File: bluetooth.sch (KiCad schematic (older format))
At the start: 63 parts, among them P16 CONN_2, P17 CONN_1, P18 CONN_1, P19 CONN_1, P20 CONN_1, P21 CONN_1, P22 CONN_1, P23 CONN_1, P24 CONN_1, P25 CONN_1, P28 CONN_1, P29 CONN_1, P30 CONN_1, P5 CONN_1, P6 CONN_1, Q1 MOSFET_N, Q3 MOSFET_N, Q4 MOS_P, Q5 MOS_P, SW3 DPST, U2 TAR5SB33, U3 HT7750A, U4 LTC4054, U5 RN42

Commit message: Add footprint of PPTC and SOD123
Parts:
- removed D2: MA721, symbol DIODE_SCHOTTKY_SOT23
- D2: renamed from D4; value RB521 -> Schottky
- renumbered D5 to D3, D3 to D4, D6 to D5, D7 to D6, D8 to D7, D9 to D8, R14 to R13, R13 to R14
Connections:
- wire segments 157 -> 153
- no-connect marks 17 -> 16
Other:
- note added: "Alt: NCP1402"
- note removed: "Schottky 30V 1A"
- moved on the sheet: D2
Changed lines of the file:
@@
 Roving Networks RN42
 $Comp
-L LED D3
+L LED D4
 U 1 1 51B43D8A
 P 5000 6400
-F 0 "D3" H 5000 6500 50  0000 C CNN
+F 0 "D4" H 5000 6500 50  0000 C CNN
 F 1 "LED" H 5000 6300 50  0000 C CNN
 F 2 "" H 5000 6400 60  0000 C CNN
@@
 Text Notes 750  4250 0    60   ~ 0
 5V Output
-NoConn ~ 2950 4350
 $Comp
 L CONN_1 P21
@@
 	1    0    0    -1
 $EndComp
-Text Notes 3900 4050 2    60   ~ 0
-Schottky 30V 1A
-$Comp
-L DIODESCH D4
+$Comp
+L DIODESCH D2
 U 1 1 51B973BC
-P 2750 3950
-F 0 "D4" H 2750 4050 40  0000 C CNN
-F 1 "RB521" H 2750 3850 40  0000 C CNN
-F 2 "" H 2750 3950 60  0000 C CNN
-F 3 "" H 2750 3950 60  0000 C CNN
-	1    2750 3950
+P 2750 4450
+F 0 "D2" H 2750 4550 40  0000 C CNN
+F 1 "Schottky" H 2750 4350 40  0000 C CNN
+F 2 "" H 2750 4450 60  0000 C CNN
+F 3 "" H 2750 4450 60  0000 C CNN
+	1    2750 4450
 	-1   0    0    1
 $EndComp
-Text Notes 4000 4200 2    60   ~ 0
-※Select one of two
-$Comp
-L LED D5
+$Comp
+L LED D3
 U 1 1 51B997A0
 P 4700 6400
-F 0 "D5" H 4700 6500 50  0000 C CNN
+F 0 "D3" H 4700 6500 50  0000 C CNN
 F 1 "LED" H 4700 6300 50  0000 C CNN
 F 2 "" H 4700 6400 60  0000 C CNN
@@
 Amp Measure
 $Comp
-L LED D6
+L LED D5
 U 1 1 51BC0B79
 P 9850 3150
-F 0 "D6" H 9850 3250 50  0000 C CNN
+F 0 "D5" H 9850 3250 50  0000 C CNN
 F 1 "LED" H 9850 3050 50  0000 C CNN
 F 2 "" H 9850 3150 60  0000 C CNN
@@
 $EndComp
 $Comp
-L LED D7
+L LED D6
 U 1 1 51BC0DCE
 P 10150 3150
-F 0 "D7" H 10150 3250 50  0000 C CNN
+F 0 "D6" H 10150 3250 50  0000 C CNN
 F 1 "LED" H 10150 3050 50  0000 C CNN
 F 2 "" H 10150 3150 60  0000 C CNN
@@
 $EndComp
 $Comp
-L R R14
+L R R13
 U 1 1 52B7F726
 P 9850 2600
-F 0 "R14" V 9930 2600 50  0000 C CNN
+F 0 "R13" V 9930 2600 50  0000 C CNN
 F 1 "470" V 9850 2600 50  0000 C CNN
 F 2 "" H 9850 2600 60  0000 C CNN
@@
 $EndComp
 $Comp
-L R R13
+L R R14
 U 1 1 52B7F735
 P 10750 2600
-F 0 "R13" V 10830 2600 50  0000 C CNN
+F 0 "R14" V 10830 2600 50  0000 C CNN
 F 1 "470" V 10750 2600 50  0000 C CNN
 F 2 "" H 10750 2600 60  0000 C CNN
@@
 $EndComp
 $Comp
-L LED D8
+L LED D7
 U 1 1 52B7FA89
 P 10750 3150
-F 0 "D8" H 10750 3250 50  0000 C CNN
+F 0 "D7" H 10750 3250 50  0000 C CNN
 F 1 "LED" H 10750 3050 50  0000 C CNN
 F 2 "" H 10750 3150 60  0000 C CNN
@@
 $EndComp
 $Comp
-L LED D9
+L LED D8
 U 1 1 52B7FA8F
 P 11050 3150
-F 0 "D9" H 11050 3250 50  0000 C CNN
+F 0 "D8" H 11050 3250 50  0000 C CNN
 F 1 "LED" H 11050 3050 50  0000 C CNN
 F 2 "" H 11050 3150 60  0000 C CNN
@@
 Text Notes 700  7250 0    60   ~ 0
 USB connected: VUSB\nUSB not connected: LIPO
-$Comp
-L DIODE_SCHOTTKY_SOT23 D2
-U 1 1 51B567E3
-P 2750 4450
-F 0 "D2" H 2750 4550 40  0000 C CNN
-F 1 "MA721" H 2800 4200 40  0000 C CNN
-F 2 "" H 2750 4450 60  0000 C CNN
-F 3 "" H 2750 4450 60  0000 C CNN
-	1    2750 4450
-	-1   0    0    1
-$EndComp
 Text Notes 6050 6400 2    60   ~ 0
 ※Select one of two
@@
 Wire Wire Line
 	3950 6350 4550 6350
-Connection ~ 2350 4450
-Wire Wire Line
-	2350 3950 2350 4450
-Wire Wire Line
-	2550 3950 2350 3950
-Connection ~ 3100 4450
-Wire Wire Line
-	3100 3950 3100 4450
-Wire Wire Line
-	2950 3950 3100 3950
 Wire Wire Line
 	6500 7400 6500 7450
@@
 Text Notes 10000 5400 0    60   ~ 0
 On: Bluetooth mode\nOff: USB mode or BT off
+Text Notes 2400 5250 0    60   ~ 0
+Alt: NCP1402
 $EndSCHEMATC

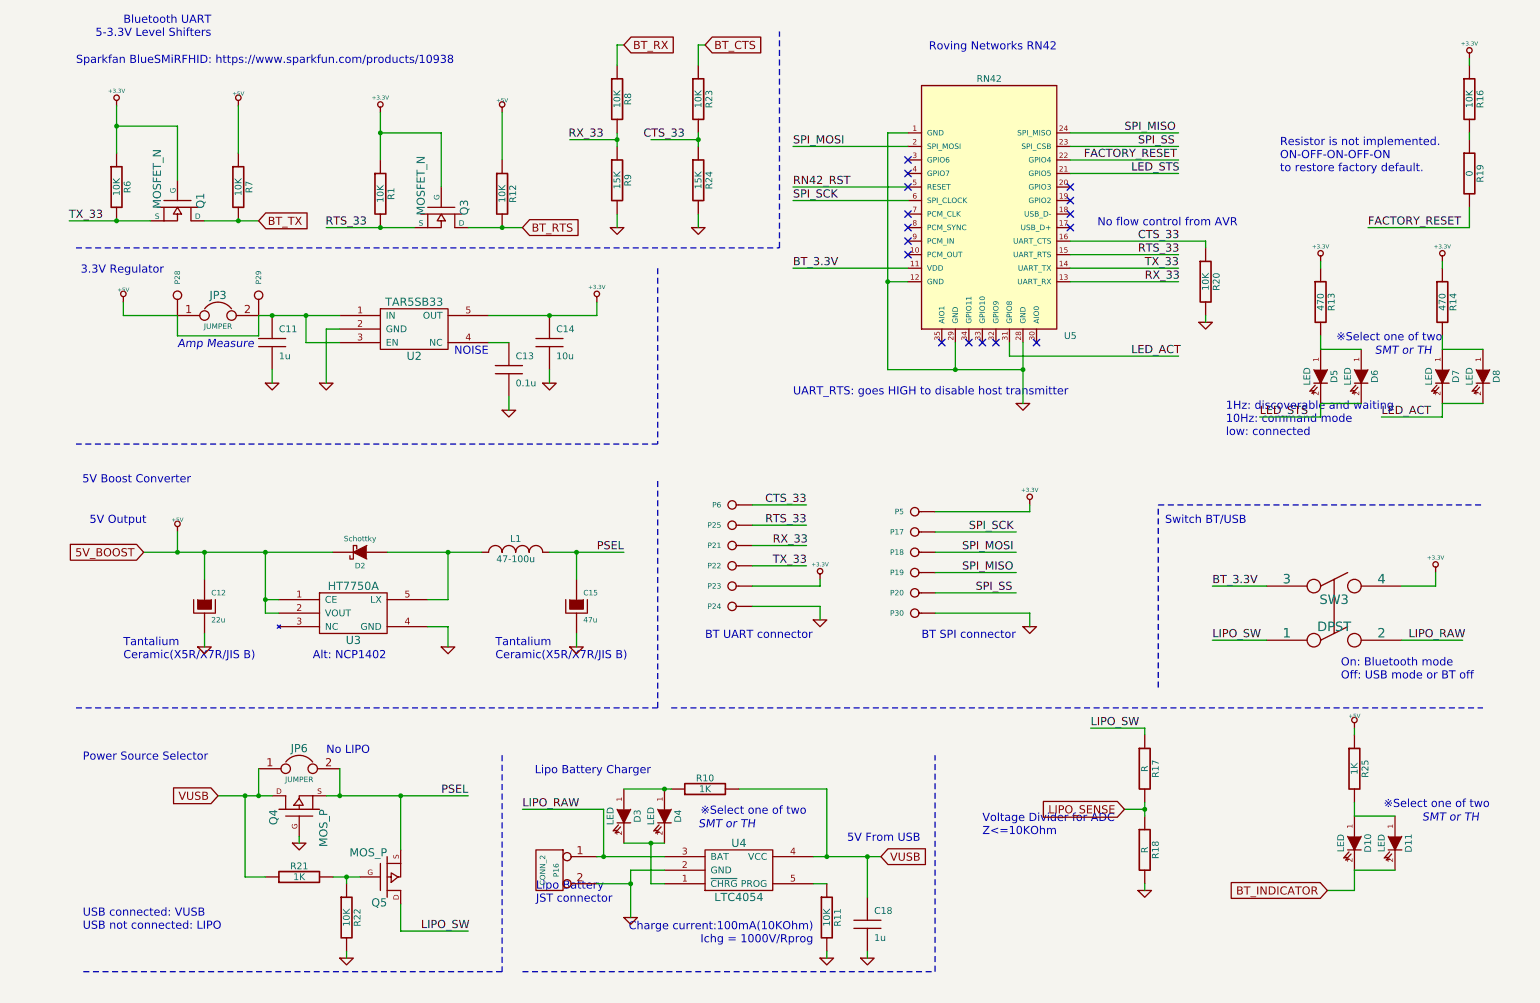
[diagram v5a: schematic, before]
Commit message: Design initial Rev.B PCB
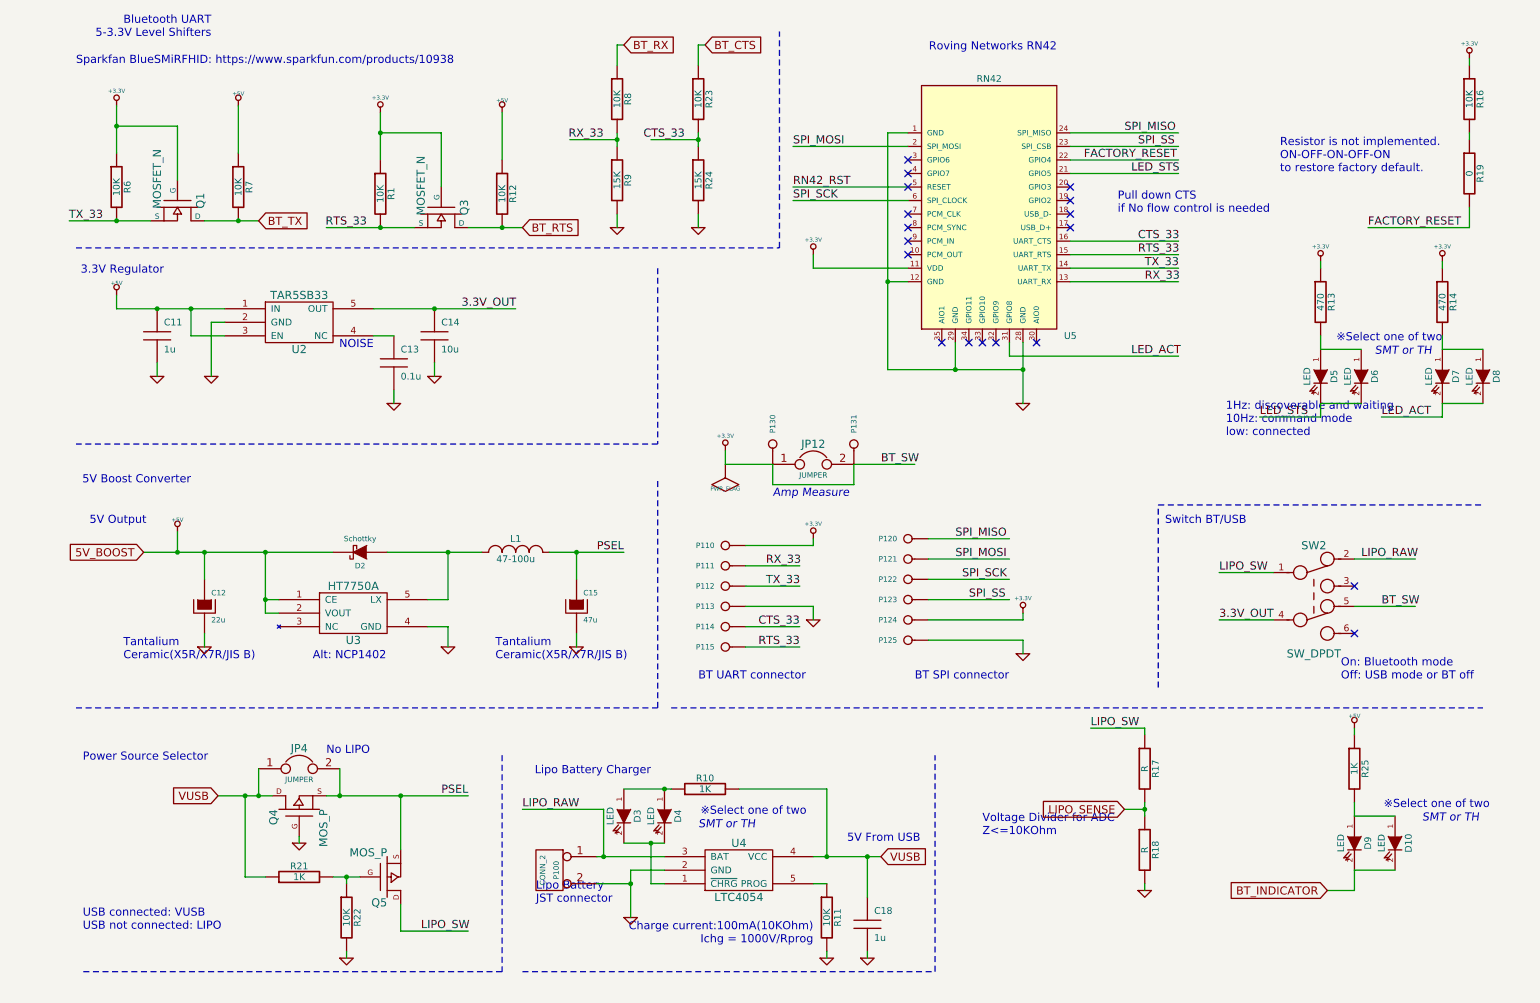
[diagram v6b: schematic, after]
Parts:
- removed R20: 10K, symbol R
- removed SW3: DPST, symbol DPST
- added SW2: SW_DPDT, symbol SW_DPDT
- renumbered D11 to D10, D10 to D9, JP3 to JP12, JP6 to JP4, P16 to P100, P23 to P110, P21 to P111, P22 to P112, P24 to P113, P6 to P114, P25 to P115, P19 to P120, P18 to P121, P17 to P122, P20 to P123, P5 to P124, P30 to P125, P28 to P130, P29 to P131
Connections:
- net labels added: 3.3V_OUT, BT_SW
- net labels removed: BT_3.3V
- wire segments 153 -> 152
- no-connect marks 16 -> 18
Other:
- note added: "Pull down CTS\nif No flow control is needed"
- note removed: "No flow control from AVR"
- note removed: "UART_RTS: goes HIGH to disable host transmitter"
- moved on the sheet: C11, C13, C14, JP12, P110, P111, P112, P113, P114, P115, P120, P121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

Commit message: Fix many fixes of rev.B errata
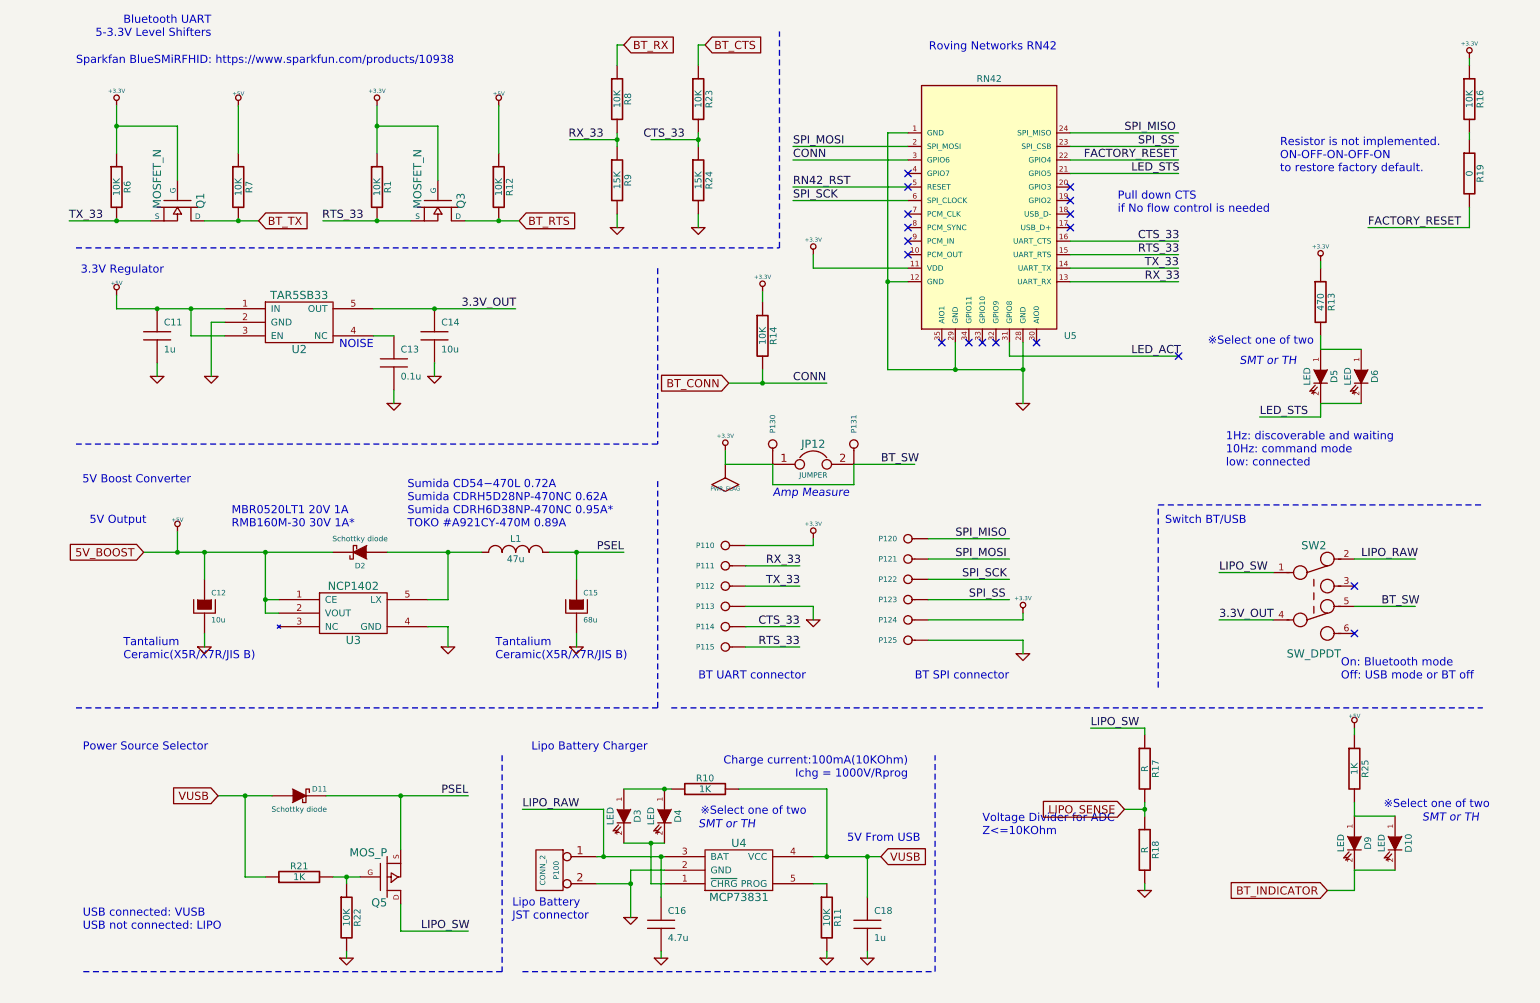
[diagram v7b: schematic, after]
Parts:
- removed D7, D8: LED, symbol LED
- removed JP4: JUMPER, symbol JUMPER
- removed Q4: MOS_P, symbol MOS_P
- added C16: 4.7u, symbol C
- added D11: Schottky diode, symbol DIODESCH
- C12: value 22u -> 10u
- C15: value 47u -> 68u
- D2: value Schottky -> Schottky diode
- L1: value 47-100u -> 47u
- R14: value 470 -> 10K
- U3: value HT7750A -> NCP1402
- U4: value LTC4054 -> MCP73831
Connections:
- net labels added: BT_CONN, CONN
- wire segments 152 -> 149
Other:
- note added: "MBR0520LT1 20V 1A\nRMB160M-30 30V 1A*"
- note added: "Sumida CD54−470L 0.72A\nSumida CDRH5D28NP-470NC 0.62A\nSumida CDRH6D38NP-470NC 0.95A*\nTOKO #A921CY-470M 0.89A"
- note removed: "Alt: NCP1402"
- note removed: "No LIPO"
- moved on the sheet: Q3, R1, R12

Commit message: Change for rev.C
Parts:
- removed D6: LED, symbol LED
- removed P120, P121, P122, P123, P124, P125: CONN_1, symbol CONN_1
- added R20: 15K, symbol R
- C18: value 1u -> 4.7u
- R19: value 0 -> F.RST
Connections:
- net labels added: LINKED, ~CHRG
- wire segments 149 -> 142
- no-connect marks 18 -> 21
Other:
- note added: "10K:10K"
- note added: "Bluetooth Module 5-3.3V Level Shifters"
- note added: "F.RST is not implemented,\nbe shorted with tweezer.\nON-OFF-ON-OFF-ON\nto restore factory default.\nPower on with turning ON."
- note added: "Hi: auto-connecting\nLo: dis-connect"
- note added: "Hi: linked"
- note added: "Hi: not charging\nLo: charging"
- note added: "JST PH2"
- note removed: "BT SPI connector"
- note removed: "Bluetooth UART\n5-3.3V Level Shifters"
- note removed: "Lipo Battery\nJST connector"
- note removed: "Pull down CTS\nif No flow control is needed"
- note removed: "Resistor is not implemented.\nON-OFF-ON-OFF-ON\nto restore factory default."
- moved on the sheet: C16, D5, JP12, P130, P131, Q1, Q3, R1, R12, R13, R14, R16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
